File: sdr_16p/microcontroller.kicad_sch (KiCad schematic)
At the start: 1 part, among them U1 RP2040

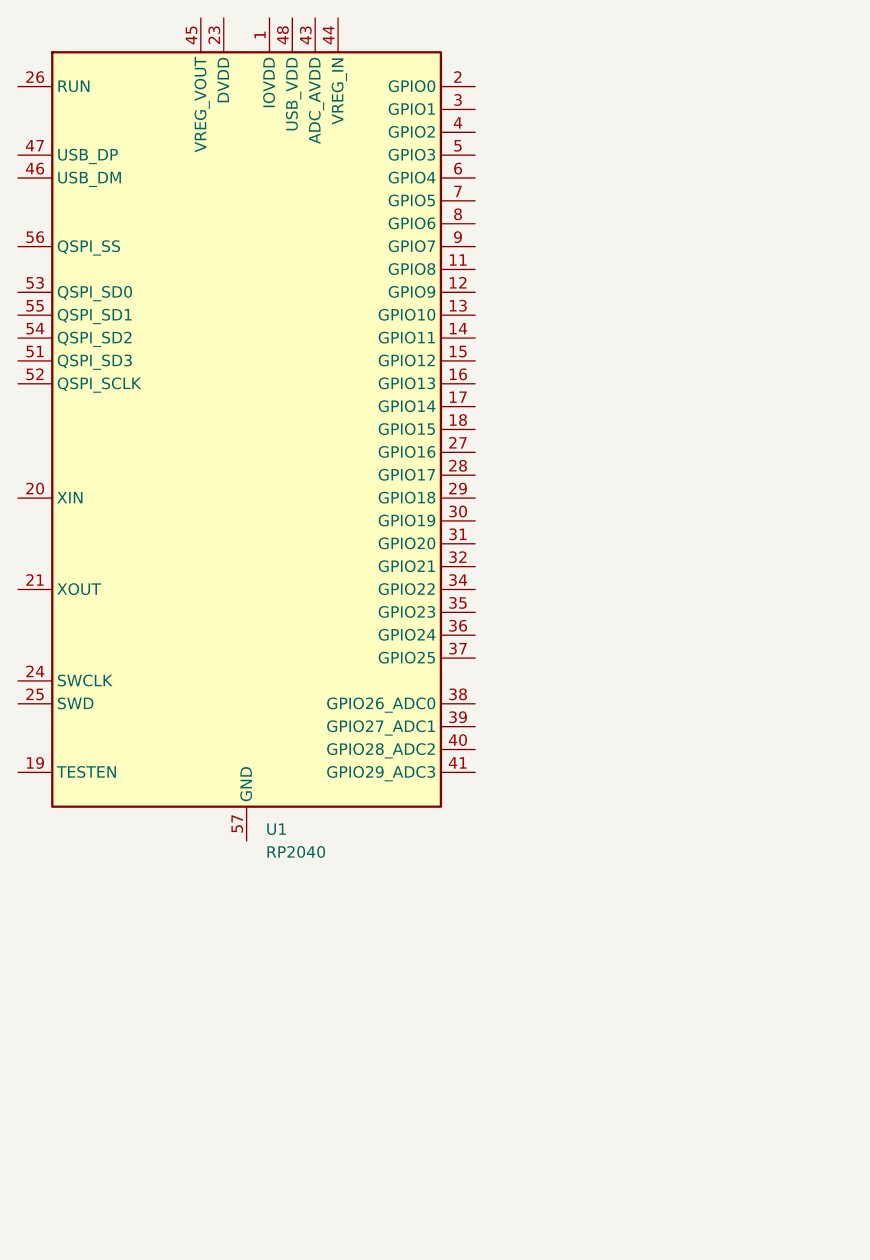
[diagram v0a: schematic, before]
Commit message: updated to 16 channel SE
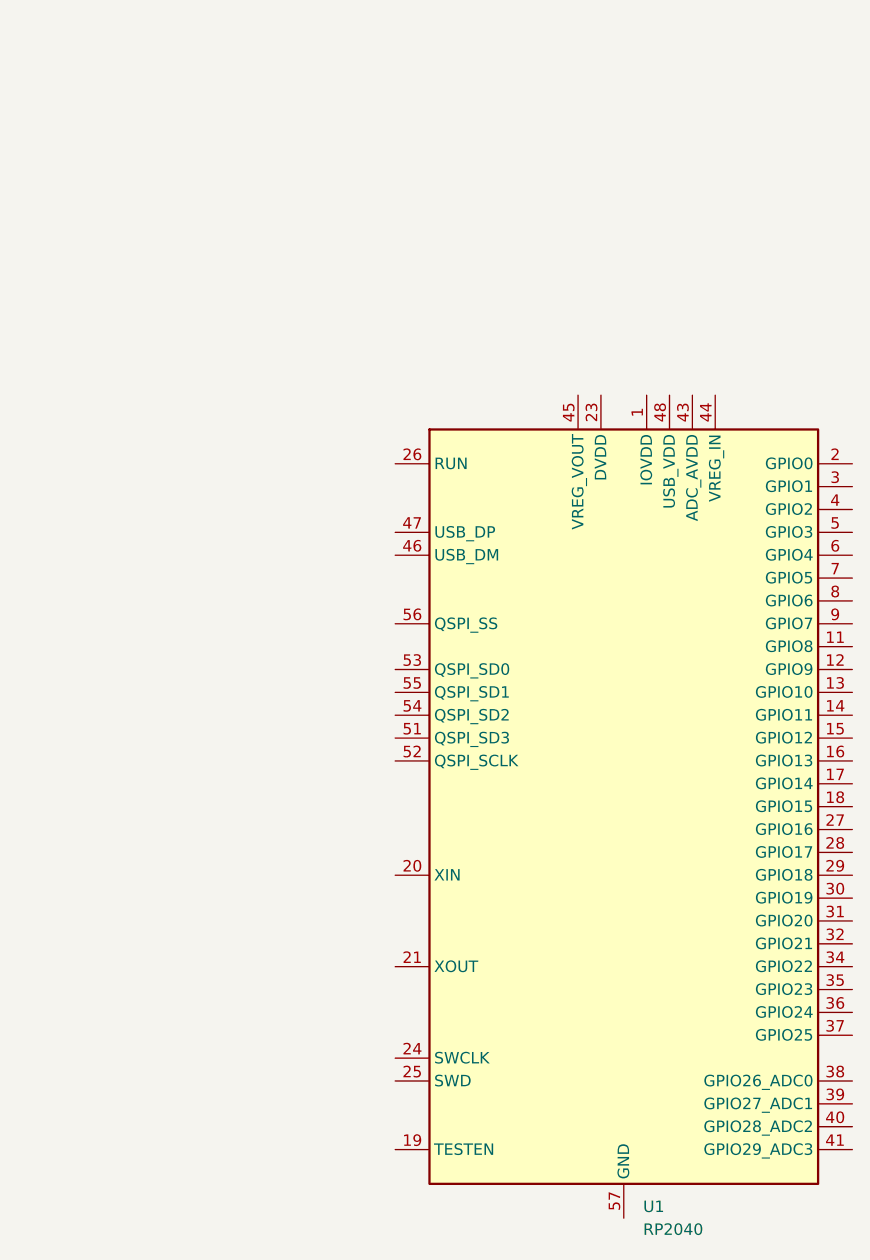
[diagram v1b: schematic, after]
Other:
- title: Microprocessor -> Microcontroller
- moved on the sheet: U1
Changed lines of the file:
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@@
 	(paper "B")
 	(title_block
-		(title "Microprocessor")
+		(title "Microcontroller")
 		(date "2026-01-02")
 		(rev "0.0")
@@
 	(symbol
 		(lib_id "MCU_RaspberryPi:RP2040")
-		(at 153.67 82.55 0)
+		(at 195.58 124.46 0)
 		(unit 1)
 		(exclude_from_sim no)
@@
 		(fields_autoplaced yes)
 		(property "Reference" "U1"
-			(at 155.8133 127 0)
+			(at 197.7233 168.91 0)
 			(effects
 				(font
@@
 		)
 		(property "Value" "RP2040"
-			(at 155.8133 129.54 0)
+			(at 197.7233 171.45 0)
 			(effects
 				(font
@@
 		)
 		(property "Footprint" "Package_DFN_QFN:QFN-56-1EP_7x7mm_P0.4mm_EP3.2x3.2mm"
-			(at 153.67 82.55 0)
+			(at 195.58 124.46 0)
 			(effects
 				(font
@@
 		)
 		(property "Datasheet" "https://datasheets.raspberrypi.com/rp2040/rp2040-datasheet.pdf"
-			(at 153.67 82.55 0)
+			(at 195.58 124.46 0)
 			(effects
 				(font
@@
 		)
 		(property "Description" "A microcontroller by Raspberry Pi"
-			(at 153.67 82.55 0)
+			(at 195.58 124.46 0)
 			(effects
 				(font
